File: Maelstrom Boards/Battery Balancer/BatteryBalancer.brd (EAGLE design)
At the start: 101.7 x 101.6 mm, 18 parts, among them P1 39-30-06?, P2 39-30-06?, P3 39-30-06?, P4 39-30-08?, P5 39-30-08?, P6 39-30-02?

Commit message: File Directory changed
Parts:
- removed P3: 39-30-06?, con-molex-mini-fit:39-30-?06?
- removed P4, P5: 39-30-08?, con-molex-mini-fit:39-30-?08?
- added C1: (no value), rcl:C0603
- added C2: (no value), rcl:E2-4
- added R1, R2, R3, R4: 100K, rcl:R0603
- P1: value 39-30-06? -> 39-30-14?; device con-molex-mini-fit:39-30-?06? -> con-molex-mini-fit:39-30-?14?
- P6: value 39-30-02? -> 39-30-16?; device con-molex-mini-fit:39-30-?02? -> con-molex-mini-fit:39-30-?16?
- moved P2 90.9 mm to (87.5, 26.6), turned to 90 degrees
- moved P1 87.3 mm to (14.7, 32.5), turned to 270 degrees
- moved P6 81.0 mm to (59.6, 87.3), turned to 180 degrees
- moved U$12 62.7 mm to (90.6, 93.8)
- moved U$4 31.2 mm to (28.1, 68.9)
- moved U$2 30.6 mm to (30.1, 82.3)
- moved U$3 25.1 mm to (17.9, 82.3)
- moved U$5 24.6 mm to (16.8, 68.8)
- moved U$6 14.9 mm to (67.0, 68.0)
- moved U$7 8.34 mm to (11.1, 94.2)
- moved U$10 1.00 mm to (58.0, 35.0)
- moved U$11 1.00 mm to (48.0, 35.0)
- moved U$8 1.00 mm to (38.0, 35.0)
- moved U$9 1.00 mm to (28.0, 35.0)
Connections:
- removed net MOTOR_POWER1: P5.1, P5.2, P5.3, P5.4, U$8.LOAD-, U$9.LOAD-
- new net GNDA: C1.2, C2.-, R3.2, R4.2, U$12.GND
- new net MOTOR_POWER: P1.1, P1.2, P1.3, P1.4, P1.5, P1.6, P1.7, U$8.LOAD-, U$9.LOAD-
- new net N$7: R1.2, R3.1, U$12.A0
- new net N$8: R1.1, R2.1, R2.2, R4.1, U$12.A1, U$12.V+
- net +3V3: now also C1.1, C2.+, U$12.VREF
- net BALANCED_OUT: now also P2.1, P2.2, P2.3; no longer P3.1, P3.2, P3.3
- net GND: now also P1.10, P1.11, P1.12, P1.13, P1.14, P1.8, P1.9, P6.10, P6.11, P6.12, P6.13, P6.14, P6.15, P6.16, P6.9; no longer P1.4, P1.5, P1.6, P3.4, P3.5, P3.6, P4.5, P4.6, P4.7, P4.8, P5.5, P5.6, P5.7, P5.8
- net KILL_SWITCH: no longer P6.1
- net MOTOR_POWER2: no longer P4.1, P4.2, P4.3, P4.4
- net PORT_BATTERY: now also P6.5, P6.6, P6.7, P6.8; no longer P1.1, P1.2, P1.3
- net STBD_BATTERY: now also P6.1, P6.2, P6.3, P6.4; no longer P2.1, P2.2, P2.3
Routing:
- net STBD_CURRENT: track 132.3 -> 0.49 mm
- net +3V3: track 94.4 -> 0.00 mm
- net BALANCED_OUT: track 85.6 -> 0.00 mm
- net MOTOR_POWER1: track 76.2 -> 0.00 mm
- net KILL_SWITCH: track 71.8 -> 0.00 mm
- net MOTOR_POWER2: track 66.4 -> 0.00 mm
- net PORT_CURRENT: track 62.8 -> 0.94 mm
- net GND: track 44.7 -> 0.00 mm
- net SENSOR_SCL: track 35.0 -> 0.00 mm
- net SENSOR_SDA: track 34.5 -> 0.30 mm
- net LOAD: track 30.0 -> 0.00 mm
- net PORT_BATTERY: track 21.2 -> 0.00 mm
- net N$4: track 22.6 -> 1.75 mm
- net STBD_BATTERY: track 15.1 -> 0.10 mm
- net N$1: track 1.27 -> 0.00 mm

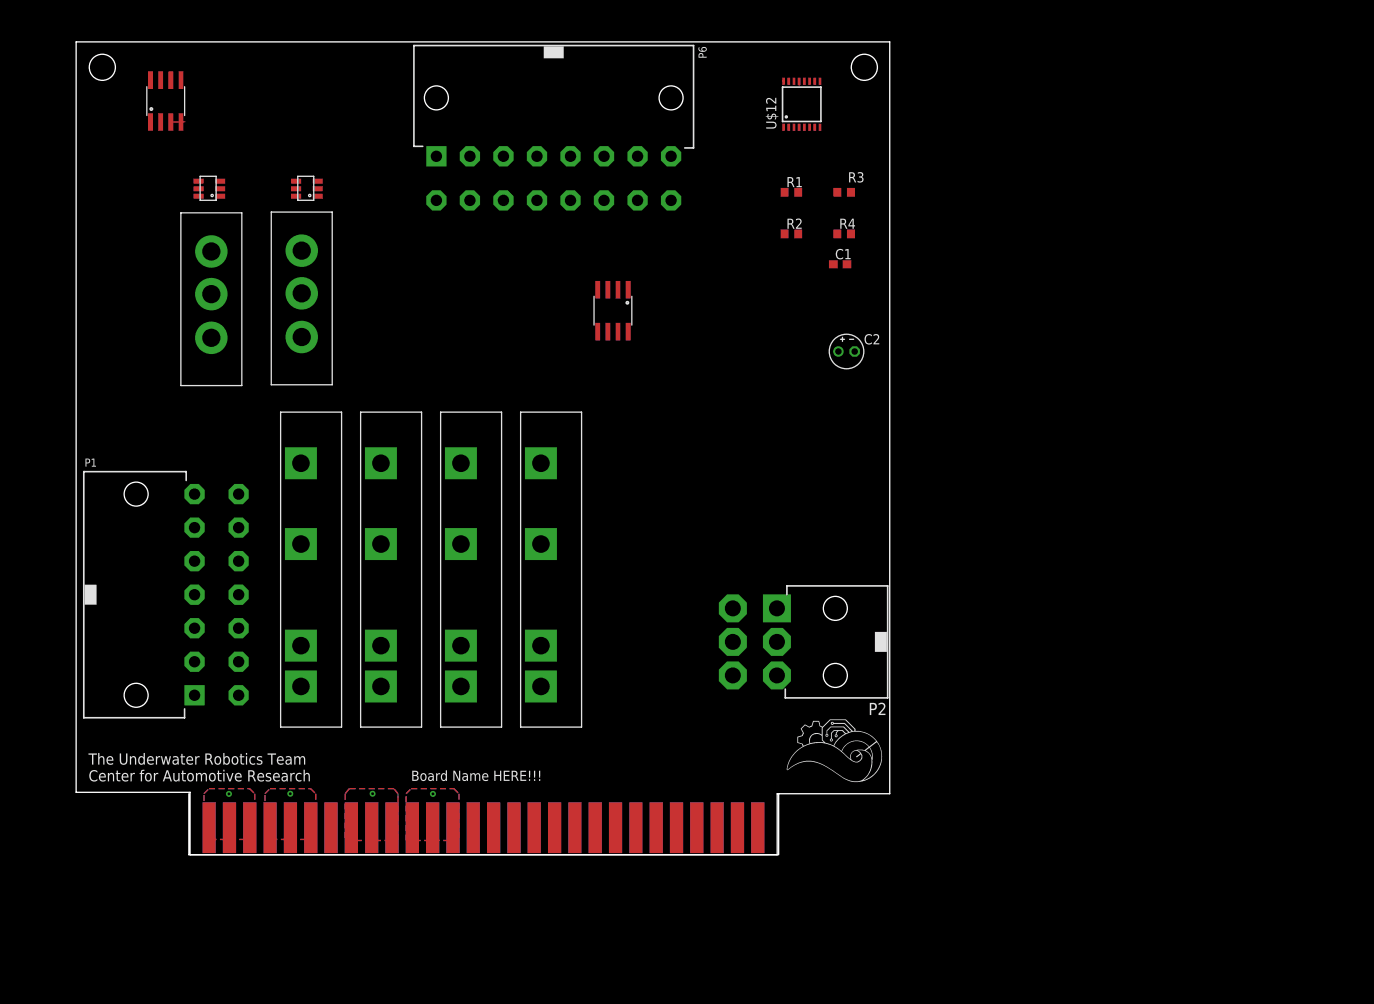
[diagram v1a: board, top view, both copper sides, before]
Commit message: updated battery balancer
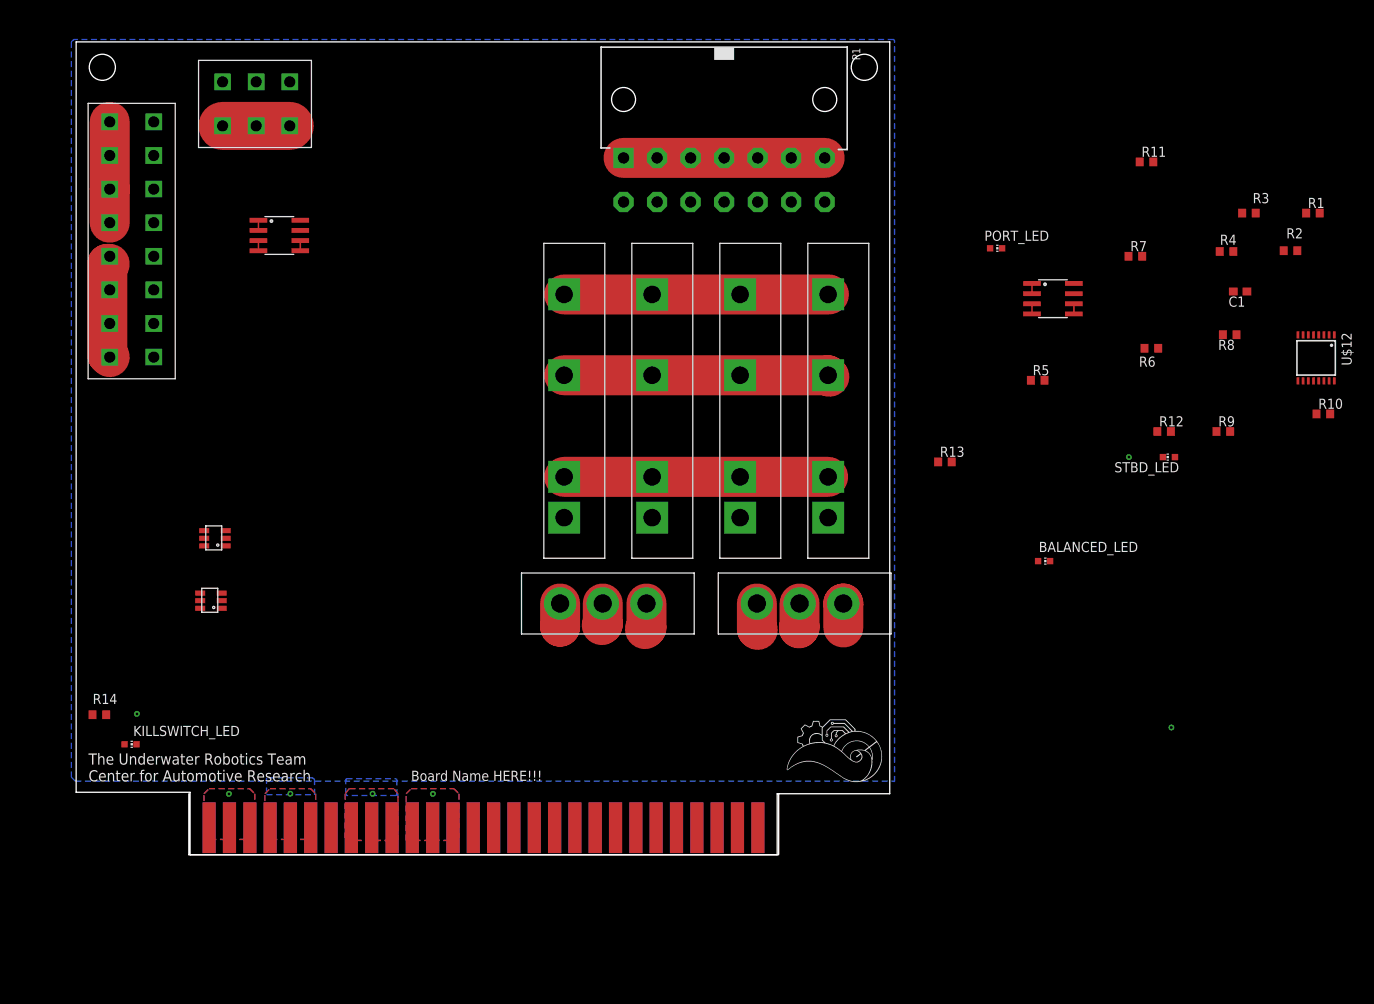
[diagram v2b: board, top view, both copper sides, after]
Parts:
- removed C2: (no value), rcl:E2-4
- removed P2: 39-30-06?, con-molex-mini-fit:39-30-?06?
- removed P6: 39-30-16?, con-molex-mini-fit:39-30-?16?
- added BALANCED_LED, KILLSWITCH_LED, PORT_LED, STBD_LED: (no value), led:CHIP-LED0603
- added R10, R6, R8: 400, rcl:R0603
- added R11, R12, R13, R14: 1450, rcl:R0603
- added R5, R7, R9: 2.6k, rcl:R0603
- added U$13: 6PIN-VERT, Vertical_Connectors:6PIN_VERT
- added U$14: 16PIN-VERT, Vertical_Connectors:16PIN_VERT
- C1: value (none) -> 0.1uF
- moved U$7 113.6 mm to (122.0, 69.5), turned to 270 degrees
- moved P1 85.8 mm to (80.9, 87.1), turned to 180 degrees
- moved U$5 83.6 mm to (91.6, 31.4), turned to 0 degrees
- moved U$12 71.7 mm to (154.9, 62.1), turned to 270 degrees
- moved R1 65.3 mm to (154.5, 80.2)
- moved R2 62.4 mm to (151.7, 75.5)
- moved U$4 54.0 mm to (67.0, 31.4), turned to 0 degrees
- moved U$3 51.5 mm to (18.1, 30.8)
- moved R3 50.7 mm to (146.5, 80.2)
- moved C1 50.1 mm to (145.4, 70.4), turned to 180 degrees
- moved R4 47.9 mm to (143.7, 75.4)
- moved U$2 45.2 mm to (18.6, 38.6)
- moved U$6 42.7 mm to (25.3, 77.4), turned to 270 degrees
- moved U$10 41.6 mm to (93.9, 56.1)
- moved U$11 40.8 mm to (82.9, 56.1)
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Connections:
- removed net LOAD: U$10.LOAD+, U$11.LOAD+, U$8.LOAD+, U$9.LOAD+
- removed net MOTOR_POWER2: U$10.LOAD-, U$11.LOAD-
- new net N$10: R8.2, R9.2, U$12.IN4
- new net N$11: PORT_LED.A, R11.2
- new net N$12: R12.2, STBD_LED.A
- new net N$13: BALANCED_LED.A, R13.1
- new net N$14: KILLSWITCH_LED.A, R14.1
- new net N$15: R5.2, R6.2, U$12.IN2
- new net N$6: R2.2, R4.1, U$12.A1
- new net N$9: R10.2, R7.2, U$12.IN3
- net +3V3: no longer C2.+
- net BALANCED_OUT: now also R13.2, R5.1, U$10.LOAD+, U$11.LOAD+, U$13.1+, U$13.2+, U$13.3+, U$8.LOAD+, U$9.LOAD+; no longer P2.1, P2.2, P2.3
- net GND: now also BALANCED_LED.C, KILLSWITCH_LED.C, PORT_LED.C, STBD_LED.C, U$13.1-, U$13.2-, U$13.3-, U$14.1-, U$14.2-, U$14.3-, U$14.4-, U$14.5-, U$14.6-, U$14.7-, U$14.7-1; no longer P2.4, P2.5, P2.6, P6.10, P6.11, P6.12, P6.13, P6.14, P6.15, P6.16, P6.9
- net GNDA: now also R10.1, R6.1, R8.1; no longer C2.-
- net KILL_SWITCH: now also R14.2
- net MOTOR_POWER: now also U$10.LOAD-, U$11.LOAD-
- net N$8: no longer R2.2, R4.1, U$12.A1
- net PORT_BATTERY: now also R11.1, R7.1, U$14.5+, U$14.6+, U$14.7+, U$14.7+1; no longer P6.5, P6.6, P6.7, P6.8
- net STBD_BATTERY: now also R12.1, R9.1, U$14.1+, U$14.2+, U$14.3+, U$14.4+; no longer P6.1, P6.2, P6.3, P6.4
- net STBD_CURRENT: now also U$12.IN1; no longer U$12.IN3
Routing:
- net MOTOR_POWER: track 0.00 -> 58.7 mm
- net BALANCED_OUT: track 0.00 -> 47.6 mm
- net KILL_SWITCH: track 0.00 -> 36.3 mm
- net PORT_BATTERY: track 0.00 -> 13.9 mm
- net STBD_BATTERY: track 0.10 -> 13.3 mm
- net N$1: track 0.00 -> 4.55 mm
- net N$5: track 0.11 -> 3.34 mm
- net GND: track 0.00 -> 3.05 mm, vias 2 -> 5
- net N$2: track 0.00 -> 2.90 mm
- net N$4: track 1.75 -> 4.27 mm
- net PORT_CURRENT: track 0.94 -> 0.00 mm

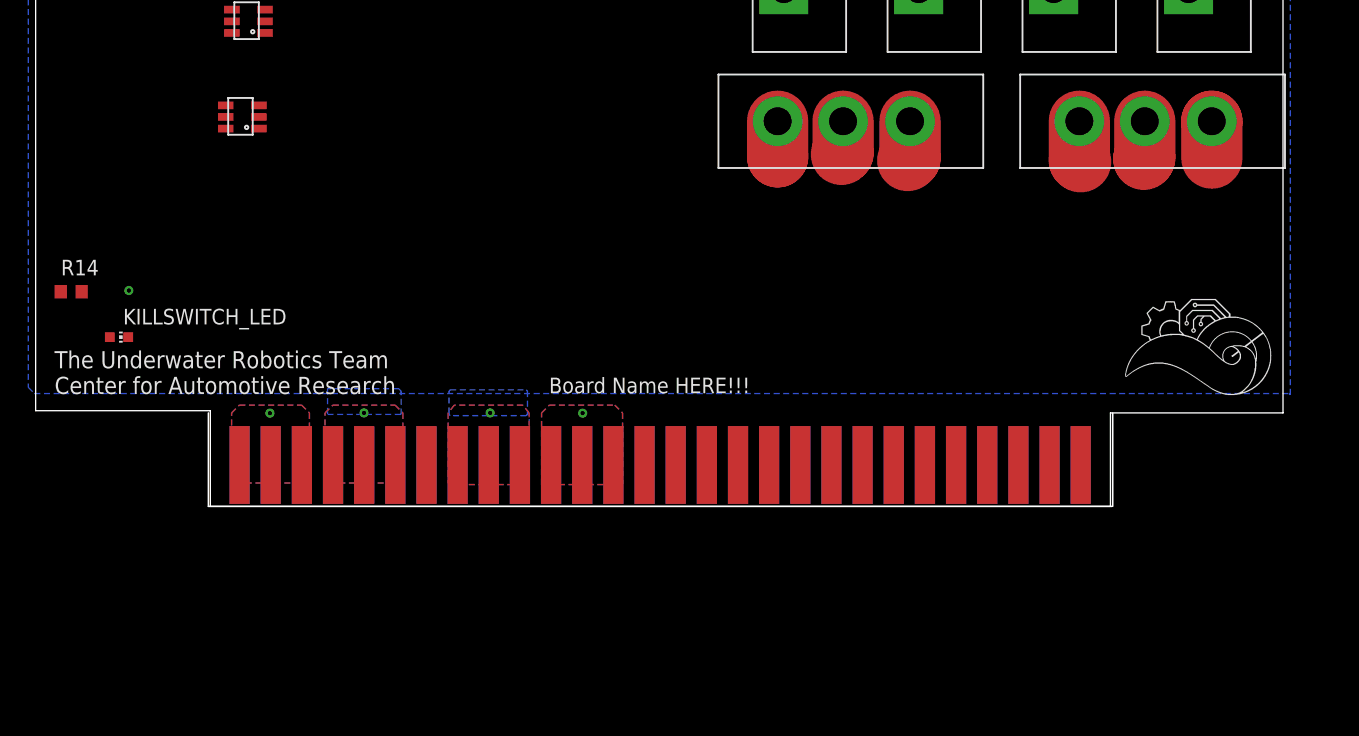
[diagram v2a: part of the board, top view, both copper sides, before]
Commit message: changed MOSFET
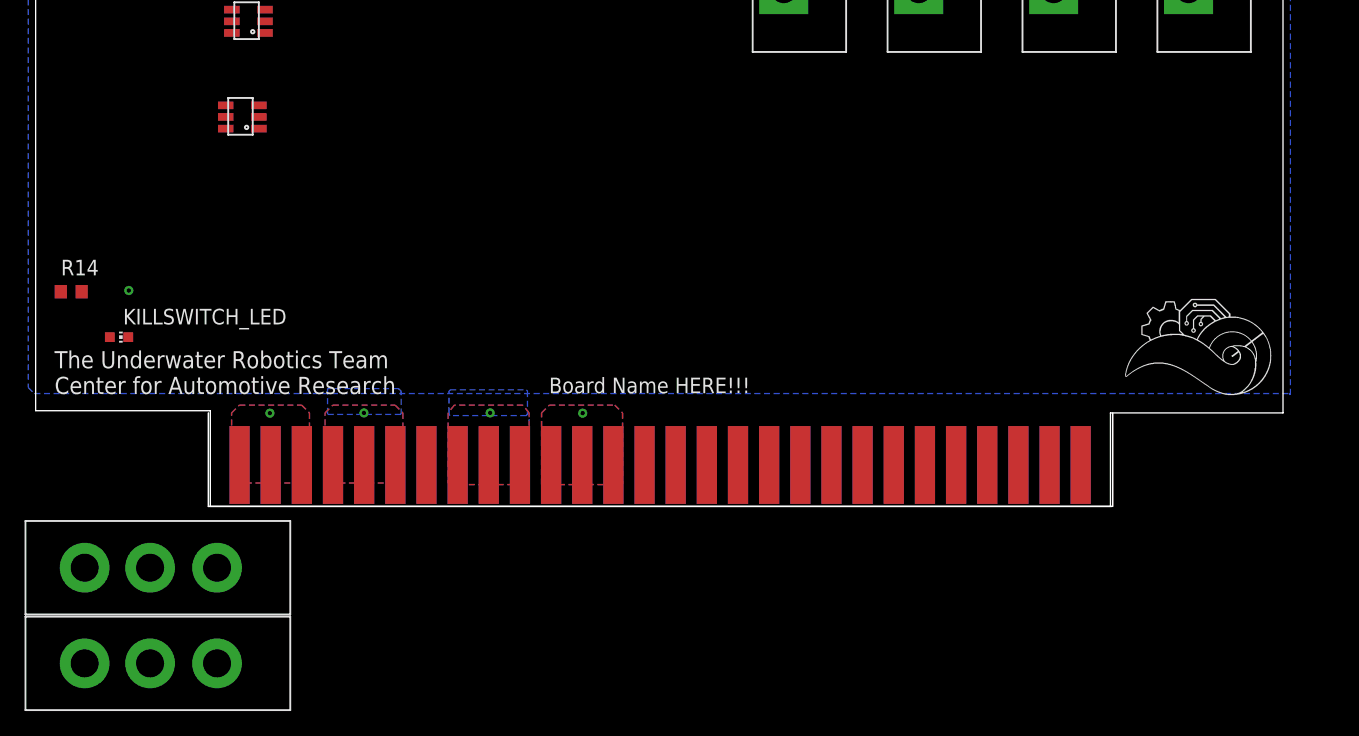
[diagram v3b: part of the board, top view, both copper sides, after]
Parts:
- removed U$4: IXFX64N60P3, IXFX64N60P3:IXFX64N60P3
- added U$15: IXFX64N60P3TK40A10N1, TK40A10N1:IXFX64N60P3
- U$5: value IXFX64N60P3 -> IXFX64N60P3TK40A10N1; device IXFX64N60P3:IXFX64N60P3 -> TK40A10N1:IXFX64N60P3
- moved U$5 88.9 mm to (10.5, -5.00)
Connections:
- net BALANCED_OUT: now also U$15.DRAIN; no longer U$4.DRAIN
- net N$1: now also U$15.SOURCE; no longer U$4.SOURCE
- net N$2: now also U$15.GATE; no longer U$4.GATE
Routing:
- net BALANCED_OUT: track 47.6 -> 41.8 mm
- net N$5: track 3.34 -> 0.00 mm
- net N$1: track 4.55 -> 1.27 mm
- net N$4: track 4.27 -> 1.27 mm
- net N$2: track 2.90 -> 0.00 mm

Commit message: worked on bard layout
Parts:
- moved U$7 100.9 mm to (21.1, 70.0)
- moved U$15 45.6 mm to (37.1, 24.2)
- moved U$5 45.6 mm to (37.1, 32.0)
- moved U$13 34.2 mm to (59.6, 82.3)
- moved U$2 16.4 mm to (34.8, 41.2), turned to 0 degrees
- moved U$3 15.0 mm to (29.5, 40.6), turned to 0 degrees
- moved U$10 5.70 mm to (88.2, 56.1)
- moved U$11 5.70 mm to (77.2, 56.1)
- moved U$8 5.70 mm to (66.2, 56.1)
- moved U$9 5.70 mm to (55.2, 56.1)
- moved U$6 5.30 mm to (21.0, 80.5)
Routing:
- net KILL_SWITCH: track 36.3 -> 79.6 mm
- net MOTOR_POWER: track 58.7 -> 97.8 mm
- net PORT_BATTERY: track 13.9 -> 6.36 mm
- net STBD_BATTERY: track 13.3 -> 6.30 mm
- added copper zone on layer 1, net PORT_BATTERY
- added copper zone on layer 1, net STBD_BATTERY
